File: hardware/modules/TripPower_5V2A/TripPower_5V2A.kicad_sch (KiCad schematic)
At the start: 0 parts

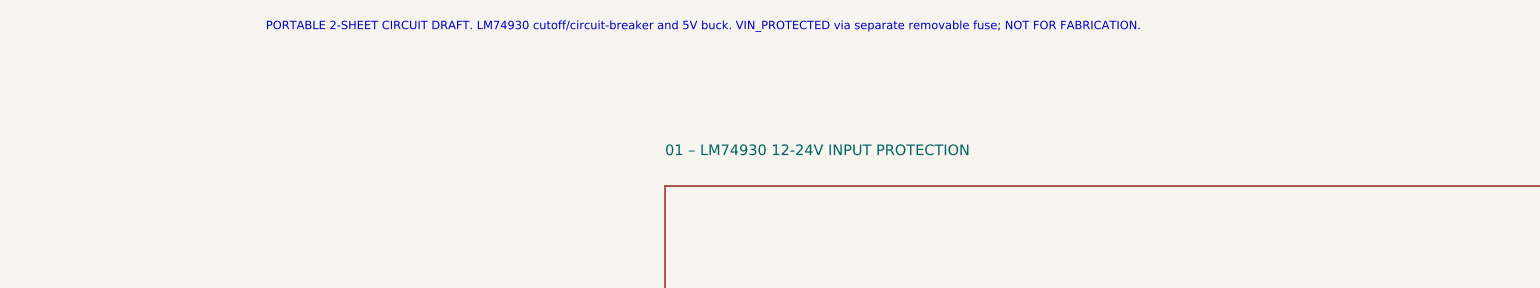
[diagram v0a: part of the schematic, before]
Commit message: hardware(TripPower): align standalone sheet and symbol library to fuse-free protected-source auxiliary output
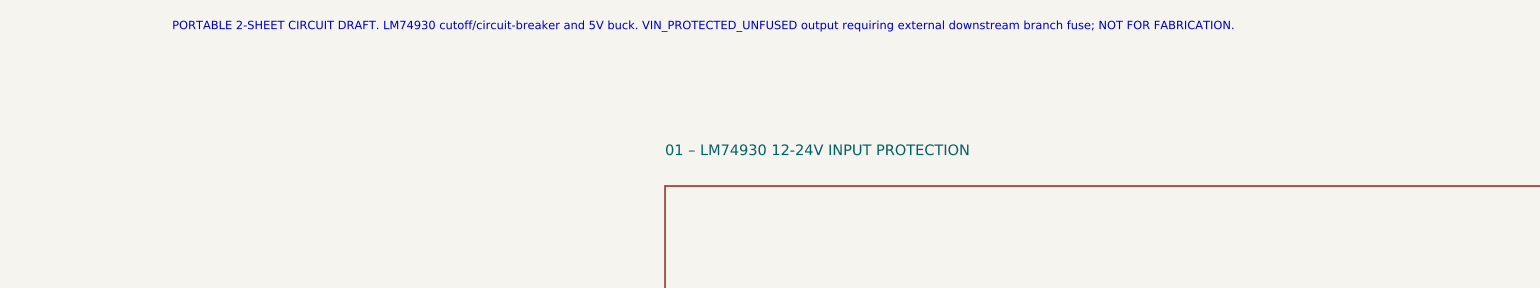
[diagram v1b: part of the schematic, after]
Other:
- note added: "PORTABLE 2-SHEET CIRCUIT DRAFT. LM74930 cutoff/circuit-breaker and 5V buck. VIN_PROTECTED_UNFUSED output requiring external downstream branch fuse; NOT FOR FABRICATION."
- note removed: "PORTABLE 2-SHEET CIRCUIT DRAFT. LM74930 cutoff/circuit-breaker and 5V buck. VIN_PROTECTED via separate removable fuse; NOT FOR FABRICATION."
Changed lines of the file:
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@@
  (paper "A4")
  (title_block (title "TripPower – universal 9-30V vehicle DC to regulated 5V/2A") (date "2026-10-14") (rev "PRELIMINARY / NOT RELEASED"))
- (text "PORTABLE 2-SHEET CIRCUIT DRAFT. LM74930 cutoff/circuit-breaker and 5V buck. VIN_PROTECTED via separate removable fuse; NOT FOR FABRICATION." (at 30 16.51 0) (effects (font (size 1.0 1.0))))
+ (text "PORTABLE 2-SHEET CIRCUIT DRAFT. LM74930 cutoff/circuit-breaker and 5V buck. VIN_PROTECTED_UNFUSED output requiring external downstream branch fuse; NOT FOR FABRICATION." (at 30 16.51 0) (effects (font (size 1.0 1.0))))
  (sheet (at 25.4 35.56) (size 215.9 40.64) (exclude_from_sim no) (in_bom yes) (on_board yes) (dnp no)
   (stroke (width 0) (type default)) (fill (color 0 0 0 0))

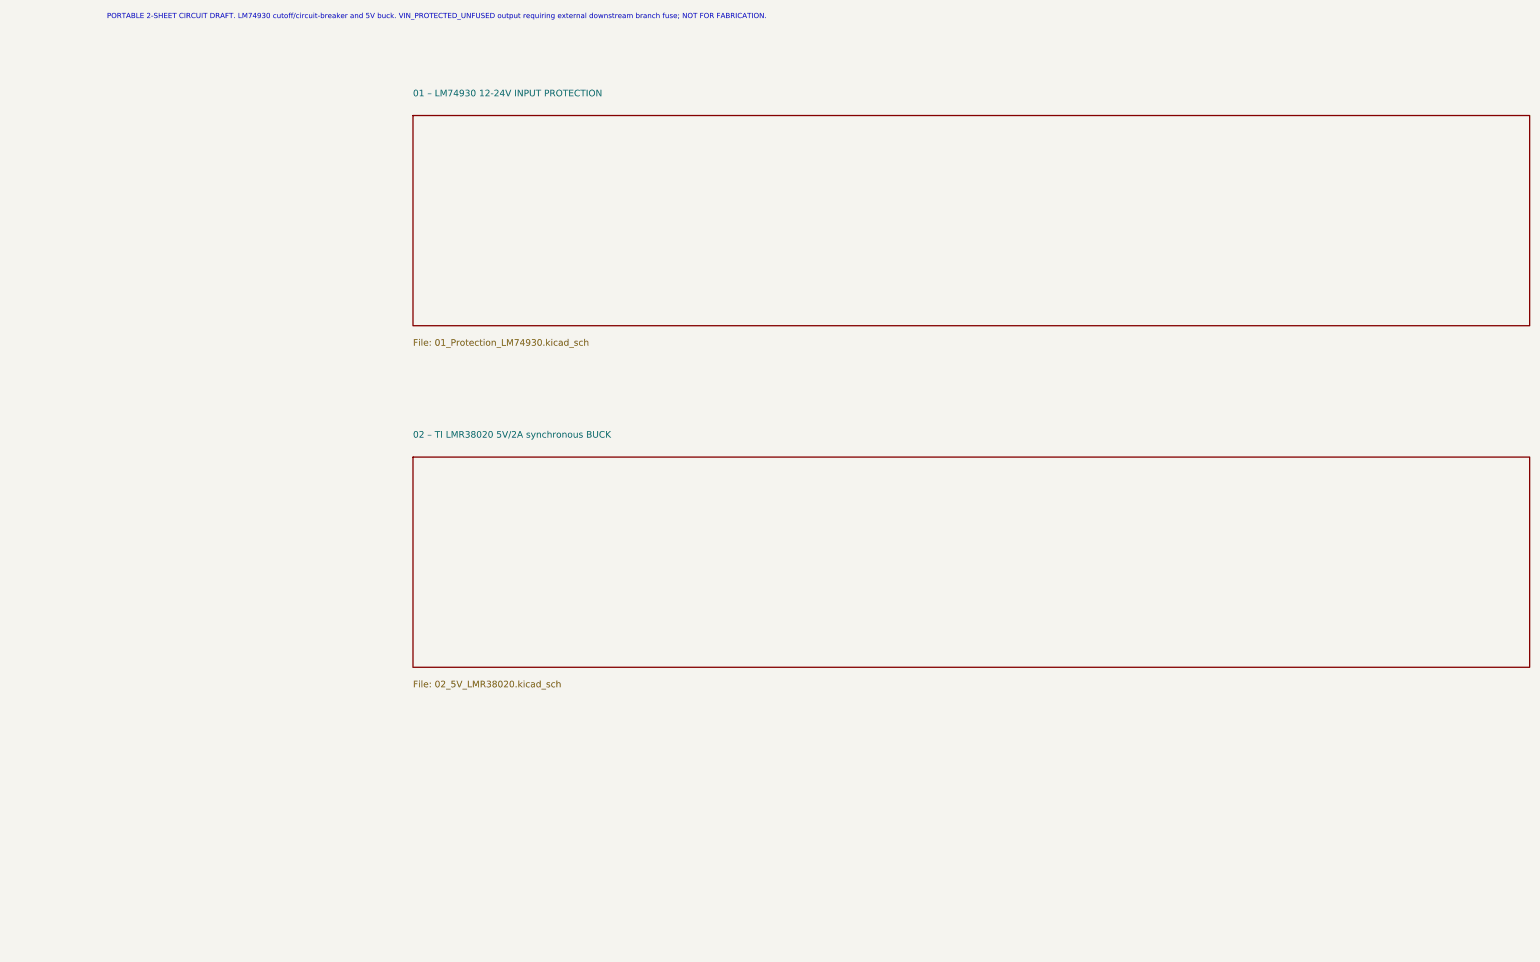
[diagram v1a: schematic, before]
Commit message: feat(TripPower): add genuine TPS3760A012DYYRQ1 U302 14-pin DYY symbol footprint and isolated 8V/6V VS_READY sheet
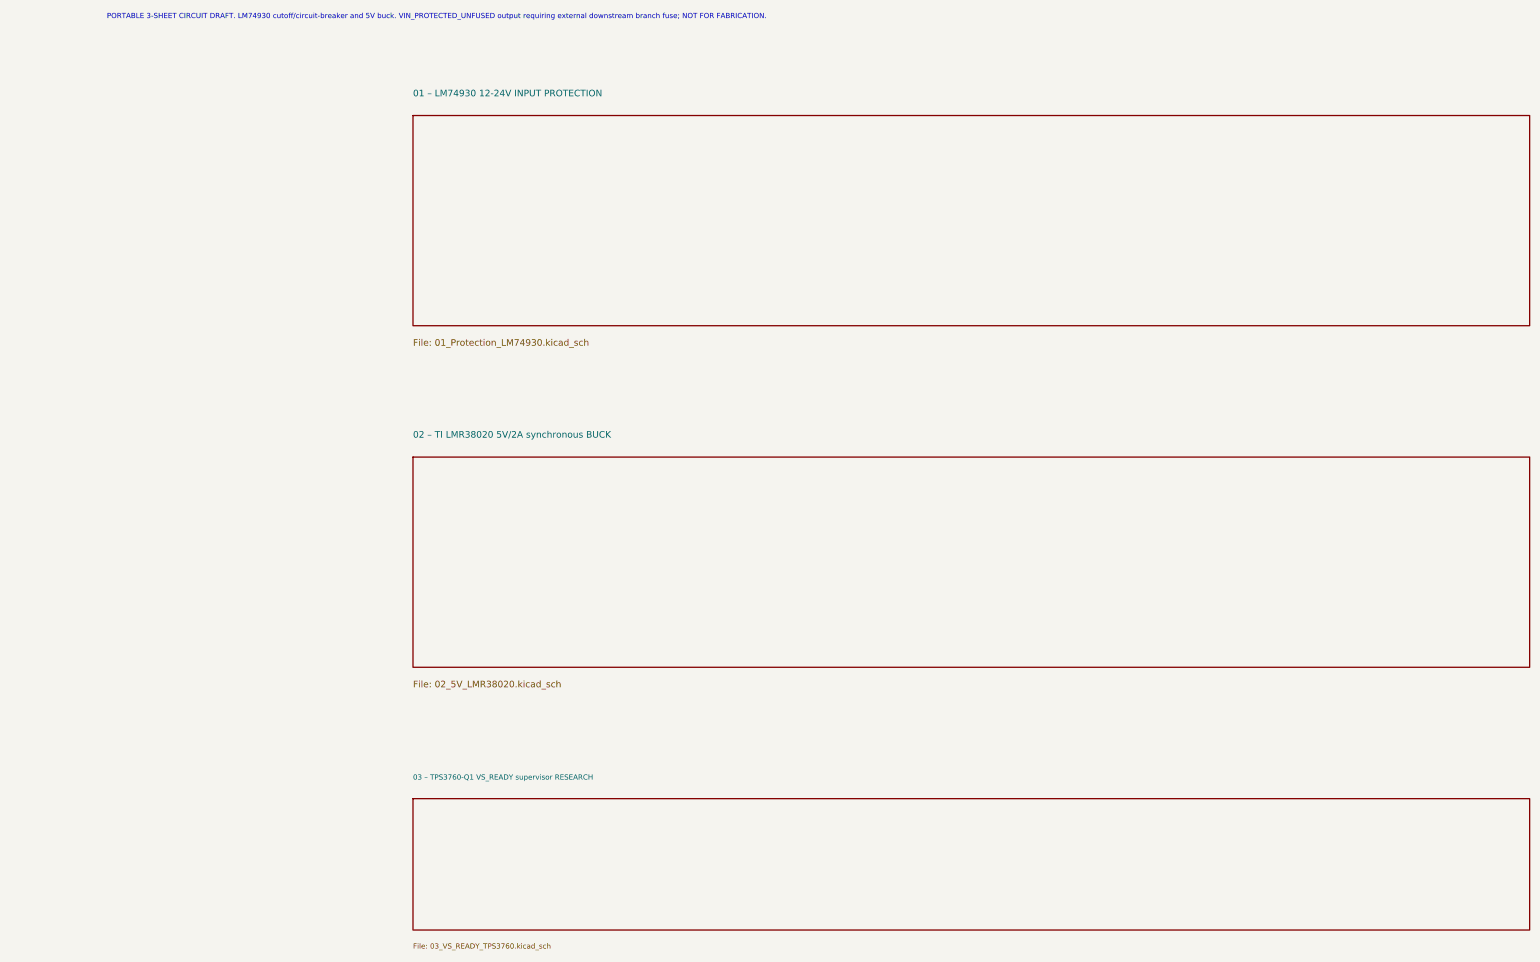
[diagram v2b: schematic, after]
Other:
- added sheet 03 – TPS3760-Q1 VS_READY supervisor RESEARCH (03_VS_READY_TPS3760.kicad_sch)
- note added: "PORTABLE 3-SHEET CIRCUIT DRAFT. LM74930 cutoff/circuit-breaker and 5V buck. VIN_PROTECTED_UNFUSED output requiring external downstream branch fuse; NOT FOR FABRICATION."
- note removed: "PORTABLE 2-SHEET CIRCUIT DRAFT. LM74930 cutoff/circuit-breaker and 5V buck. VIN_PROTECTED_UNFUSED output requiring external downstream branch fuse; NOT FOR FABRICATION."
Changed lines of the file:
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@@
  (paper "A4")
  (title_block (title "TripPower – universal 9-30V vehicle DC to regulated 5V/2A") (date "2026-10-14") (rev "PRELIMINARY / NOT RELEASED"))
- (text "PORTABLE 2-SHEET CIRCUIT DRAFT. LM74930 cutoff/circuit-breaker and 5V buck. VIN_PROTECTED_UNFUSED output requiring external downstream branch fuse; NOT FOR FABRICATION." (at 30 16.51 0) (effects (font (size 1.0 1.0))))
+ (text "PORTABLE 3-SHEET CIRCUIT DRAFT. LM74930 cutoff/circuit-breaker and 5V buck. VIN_PROTECTED_UNFUSED output requiring external downstream branch fuse; NOT FOR FABRICATION." (at 30 16.51 0) (effects (font (size 1.0 1.0))))
  (sheet (at 25.4 35.56) (size 215.9 40.64) (exclude_from_sim no) (in_bom yes) (on_board yes) (dnp no)
   (stroke (width 0) (type default)) (fill (color 0 0 0 0))
@@
   (property "Sheetfile" "02_5V_LMR38020.kicad_sch" (at 25.4 144.78 0) (effects (font (size 1.27 1.27)) (justify left top)))
   (instances (project "TripPower_5V2A" (path "/f1512578-cc72-4c26-bf70-dbbd00000001" (page "3")))))
+(sheet (at 25.4 167.64) (size 215.9 25.4) (exclude_from_sim no) (in_bom yes) (on_board yes) (dnp no)
+(stroke (width 0) (type default)) (fill (color 0 0 0 0))
+(property "Sheetname" "03 – TPS3760-Q1 VS_READY supervisor RESEARCH" (at 25.4 164.08 0) (effects (font (size 1 1)) (justify left bottom)))
+(property "Sheetfile" "03_VS_READY_TPS3760.kicad_sch" (at 25.4 195.58 0) (effects (font (size 1 1)) (justify left top)))
+(instances (project "TripPower_5V2A" (path "/f1512578-cc72-4c26-bf70-dbbd00000001" (page "4")))))
  (embedded_fonts no))
